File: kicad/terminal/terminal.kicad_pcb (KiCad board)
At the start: 2 copper layers, 101.6 x 38.1 mm, 33 parts, among them J1 USB, J2 PS2, J3 VGA, J5 Serial, J6 External 5V, J7 ICSP, U1 PIC32MX270F256B-I_SP, U2 MCP1700-3302E_TO92, Y1 20MHz

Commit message: ground planes instead of traces, fatter traces for power
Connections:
- J1 pad 5: Net-(J1-Pad5) -> GND
- J2 pad S1: (no net) -> GND
- J2 pad S2: (no net) -> GND
- J2 pad S3: (no net) -> GND
- J3 pad S1: (no net) -> GND
- J3 pad S2: (no net) -> GND
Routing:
- net GND: track 192.8 -> 0.00 mm
- net Net-(J1-Pad5): track 12.0 -> 0.00 mm
- net USB_D+: track 37.8 -> 31.6 mm
- net USB_D-: track 35.8 -> 30.2 mm
- net SERIAL_TXD: track 39.1 -> 35.8 mm
- net +5V: track 135.8 -> 138.6 mm
- net Net-(C6-Pad1): track 66.4 -> 69.0 mm
- net Net-(C7-Pad1): track 59.8 -> 62.3 mm
- net VGA_VSYNCH: track 39.6 -> 41.8 mm
- net Net-(J3-Pad1): track 10.9 -> 13.1 mm
- net PS2_CLK: track 77.5 -> 79.6 mm
- net VCC: track 130.8 -> 132.9 mm
- net PS2_DATA: track 45.7 -> 47.2 mm
- net Net-(J5-Pad3): track 58.7 -> 59.9 mm
- net Net-(J3-Pad2): track 11.3 -> 12.5 mm
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- added copper zone on B.Cu, net GND
- added copper zone on F.Cu, net GND
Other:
- net class Default: clearance 0.2 -> 0.1778; trace_width 0.25 -> 0.254; via_dia 0.8 -> 0.4064; via_drill 0.4 -> 0.254
- rule pad_to_mask_clearance: 0.051 -> 0
- rule solder_mask_min_width: 0.25 -> 0.1778
- rule trace_clearance: 0.2 -> 0.1778
- rule trace_min: 0.2 -> 0.1524
- rule via_min_drill: 0.3 -> 0.254
- rule via_min_size: 0.4 -> 0.4064
- board text added: "ASCII Terminal Version 2.0-bkw (C) 2014-2019 Geoff Graham and Peter Hizalev 2020 Brian K. White - github.com/bkw777/terminal"
- board text removed: "ASCII Terminal Version 2.0 (C) 2014-2019 Geoff Graham and Peter Hizalev https://github.com/petrohi/terminal"

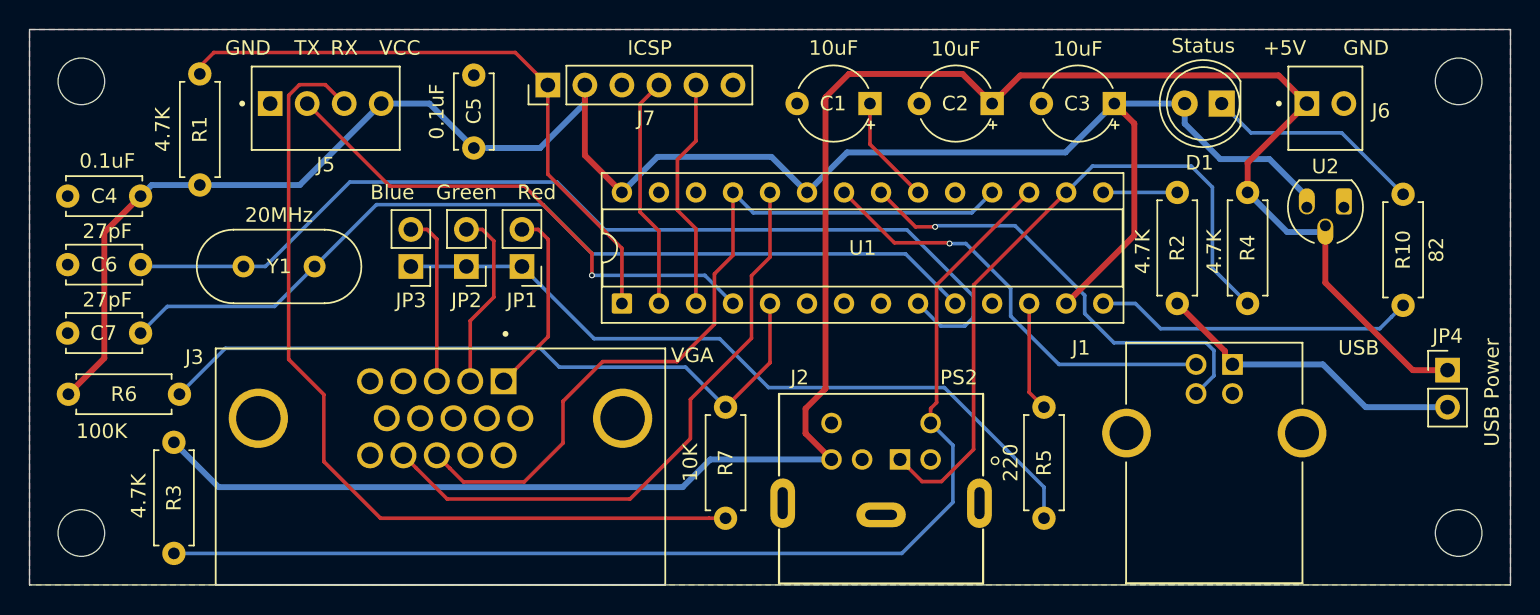
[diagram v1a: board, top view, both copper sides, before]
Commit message: footprint tweaks
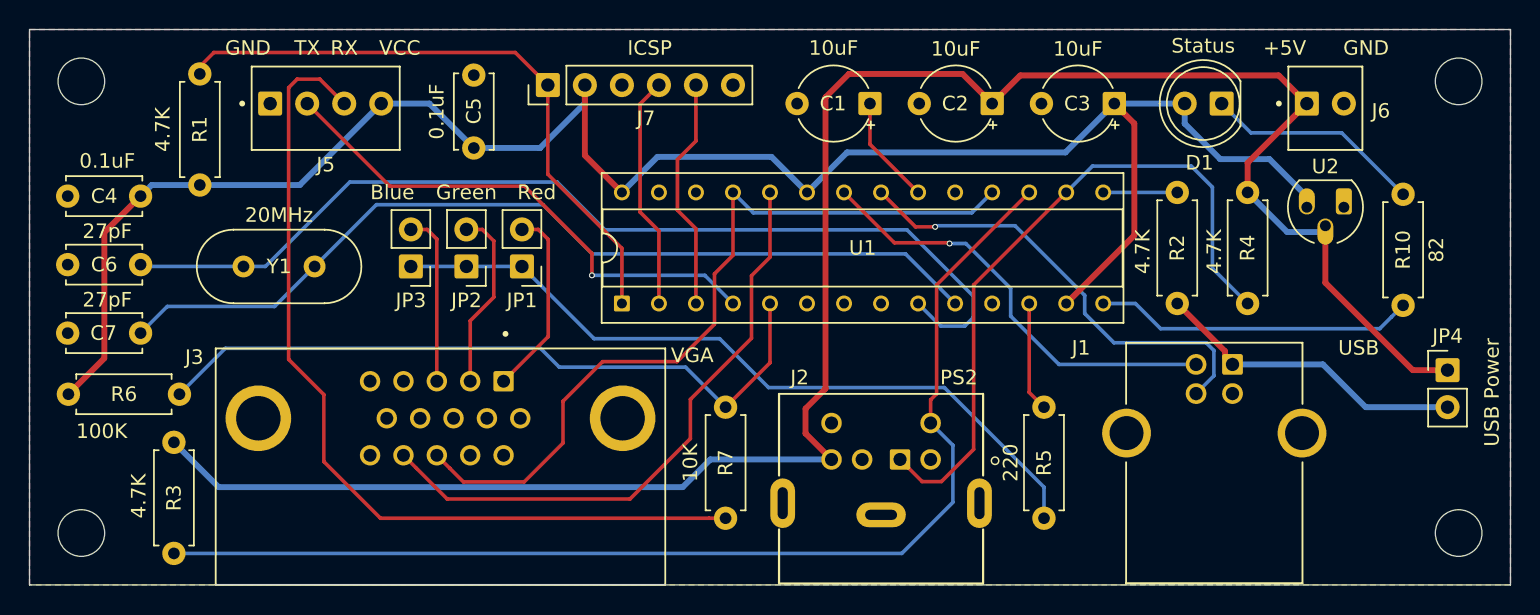
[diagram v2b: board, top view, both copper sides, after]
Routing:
- net Net-(J5-Pad3): track 59.9 -> 60.6 mm
